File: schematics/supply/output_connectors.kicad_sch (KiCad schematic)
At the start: 16 parts, among them J16 banana jack + fuse 20A, J17 Conn_02x04_Odd_Even, J18 banana jack + fuse 15A, J19 jst xh angle, J20 jst xh angle, Q10 IRLML0030, Q10 IRLML5203

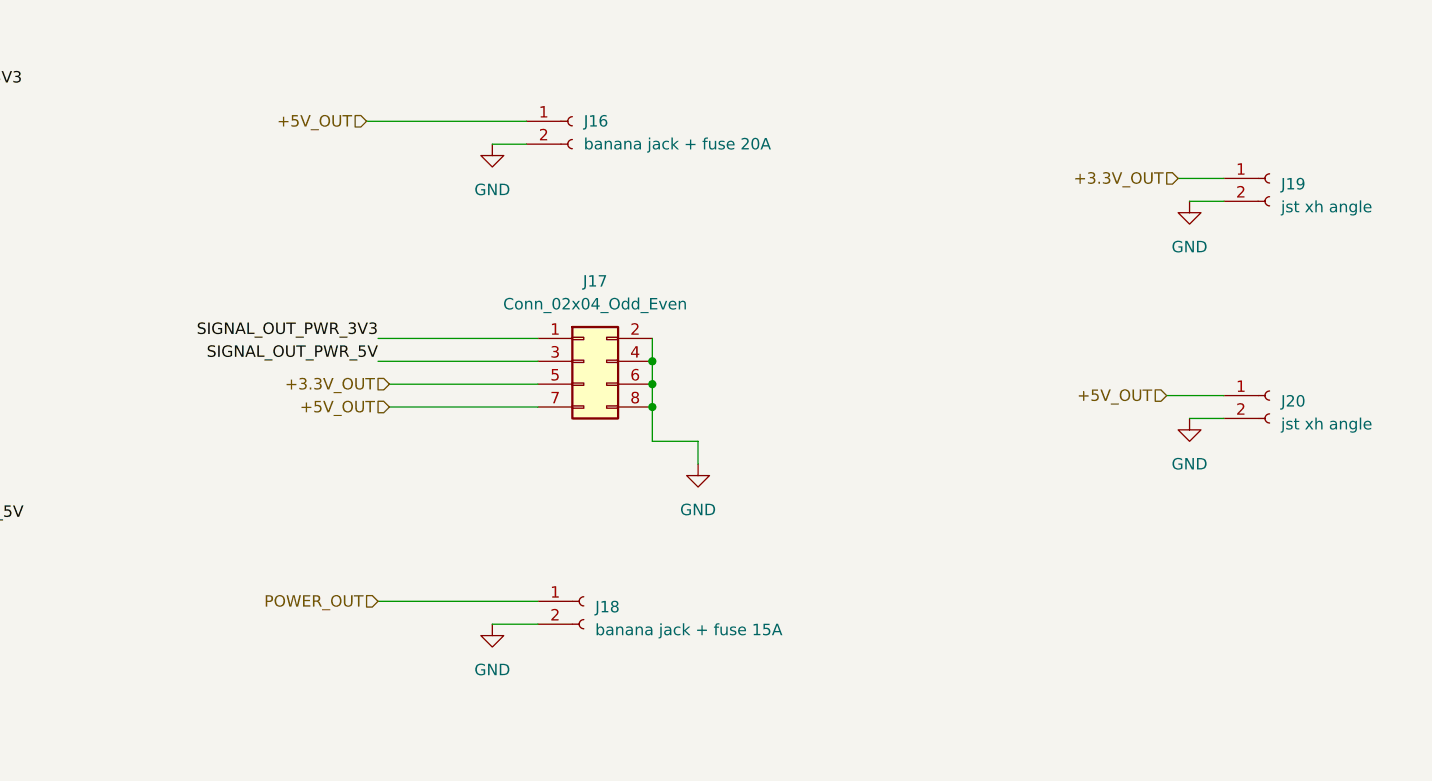
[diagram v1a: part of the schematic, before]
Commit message: Prepare to move USB ports to a few millimenters outside
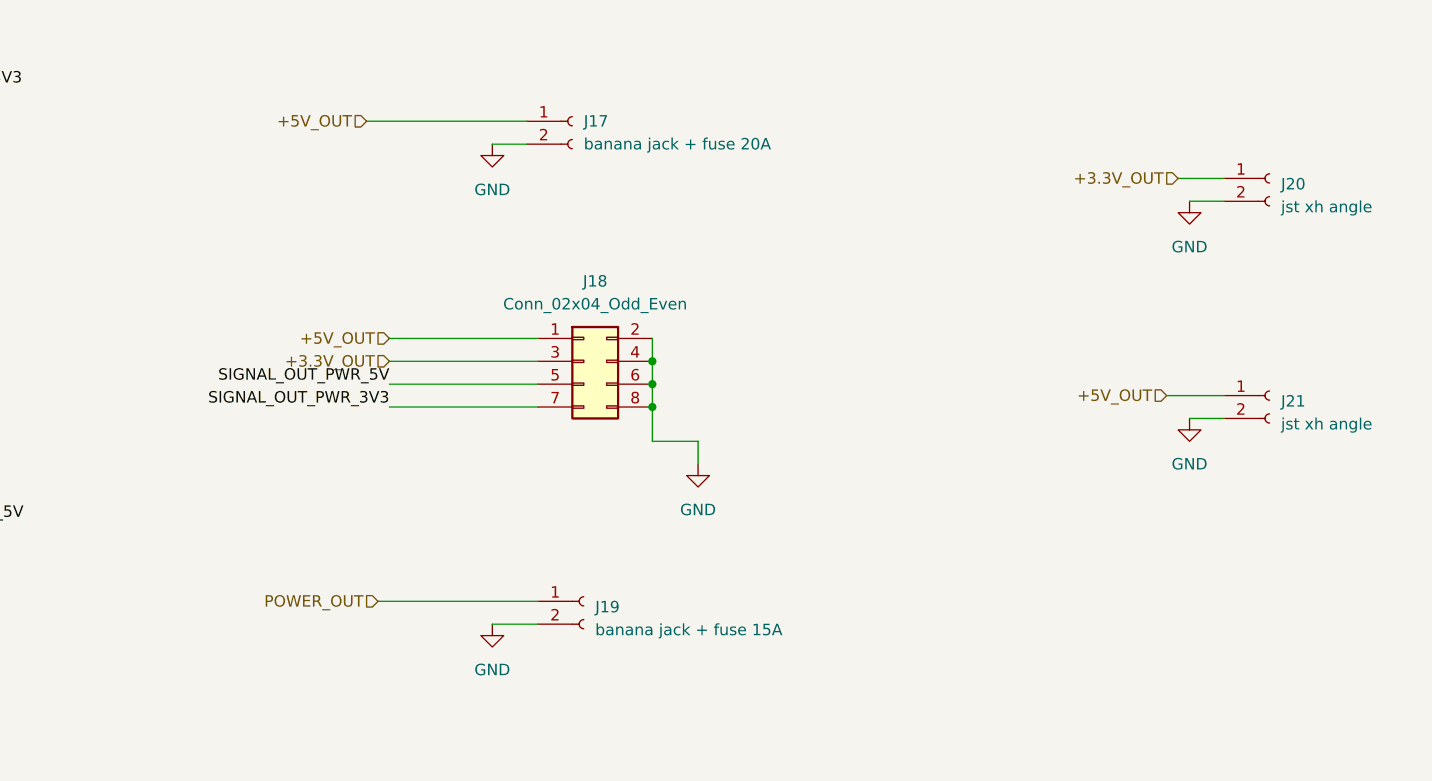
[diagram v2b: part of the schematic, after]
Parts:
- J18: renamed from J17; footprint Connector_PinHeader_2.54mm:PinHeader_2x04_P2.54mm_Vertical -> Connector_PinSocket_2.54mm:PinSocket_2x04_P2.54mm_Horizontal
- renumbered J16 to J17, J18 to J19, J19 to J20, J20 to J21
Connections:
- net +3.3V_OUT: now also J18.3 (Pin_3); no longer J18.5 (Pin_5)
- net +5V_OUT: now also J18.1 (Pin_1); no longer J18.7 (Pin_7)
- net SIGNAL_OUT_PWR_3V3: now also J18.7 (Pin_7); no longer J18.1 (Pin_1)
- net SIGNAL_OUT_PWR_5V: now also J18.5 (Pin_5); no longer J18.3 (Pin_3)

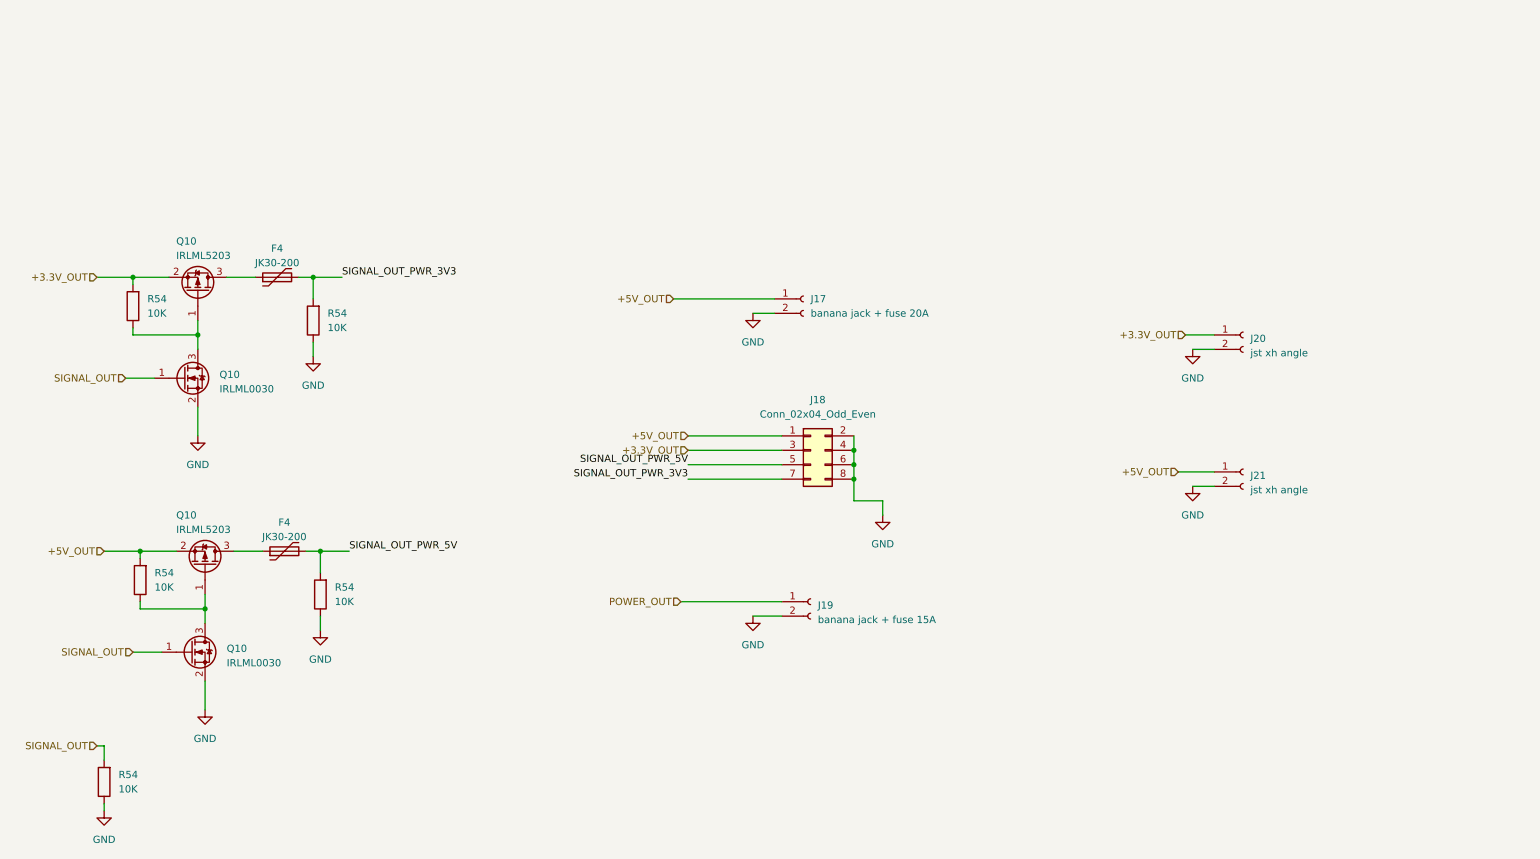
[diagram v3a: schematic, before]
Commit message: prepare to add current measurement for a middle-current 5V and 3.3V lines
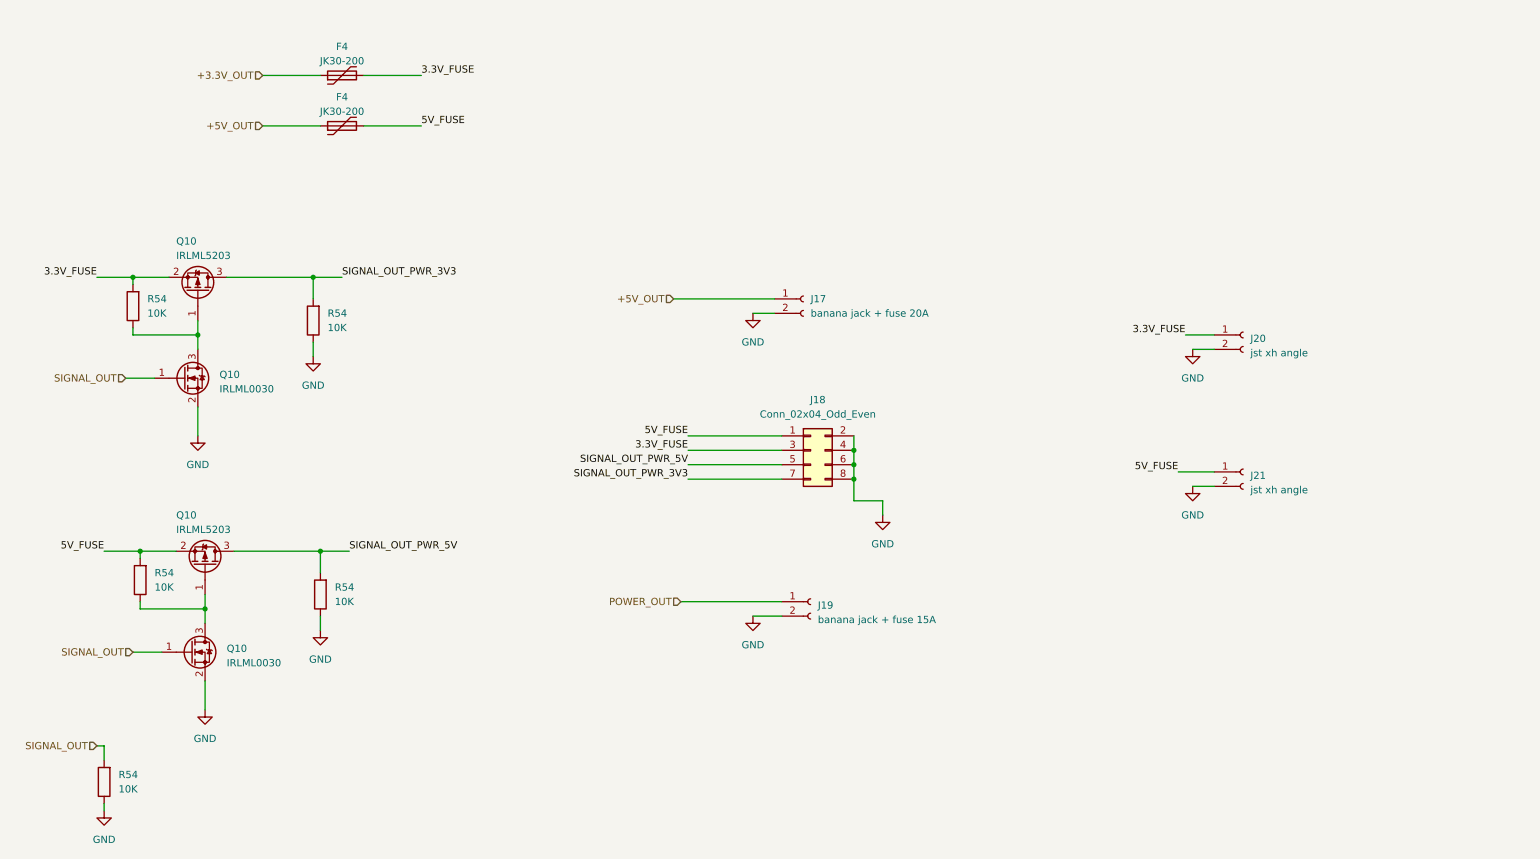
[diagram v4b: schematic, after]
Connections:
- net +3.3V_OUT: now also F4.1; no longer J18.3 (Pin_3), J20.1 (Pin_1), Q10.2 (S), R54.2
- net +5V_OUT: now also F4.1; no longer J18.1 (Pin_1), J21.1 (Pin_1), Q10.2 (S), R54.2
- net SIGNAL_OUT_PWR_3V3: now also Q10.3 (D); no longer F4.2
- net SIGNAL_OUT_PWR_5V: now also Q10.3 (D); no longer F4.2
- new net 3.3V_FUSE: F4.2, J18.3 (Pin_3), J20.1 (Pin_1), Q10.2 (S), R54.2
- new net 5V_FUSE: F4.2, J18.1 (Pin_1), J21.1 (Pin_1), Q10.2 (S), R54.2
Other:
- moved on the sheet: F4
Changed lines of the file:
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@@
   (junction (at 38.1 111.76) (diameter 0) (color 0 0 0 0)
   )
+  (junction (at 68.58 63.5) (diameter 0) (color 0 0 0 0)
+  )
   (junction (at 163.83 99.06) (diameter 0) (color 0 0 0 0)
   )
   (junction (at 163.83 96.52) (diameter 0) (color 0 0 0 0)
   )
-  (junction (at 68.58 63.5) (diameter 0) (color 0 0 0 0)
-  )
   (junction (at 49.53 121.92) (diameter 0) (color 0 0 0 0)
   )
@@
     (stroke (width 0) (type default))
   )
-  (wire (pts (xy 54.61 111.76) (xy 59.69 111.76))
+  (wire (pts (xy 59.69 36.83) (xy 69.85 36.83))
     (stroke (width 0) (type default))
   )
@@
     (stroke (width 0) (type default))
   )
+  (wire (pts (xy 54.61 111.76) (xy 69.85 111.76))
+    (stroke (width 0) (type default))
+  )
   (wire (pts (xy 134.62 91.44) (xy 151.13 91.44))
     (stroke (width 0) (type default))
@@
     (stroke (width 0) (type default))
   )
+  (wire (pts (xy 59.69 27.94) (xy 69.85 27.94))
+    (stroke (width 0) (type default))
+  )
   (wire (pts (xy 68.58 63.5) (xy 73.66 63.5))
     (stroke (width 0) (type default))
@@
     (stroke (width 0) (type default))
   )
+  (wire (pts (xy 77.47 27.94) (xy 87.63 27.94))
+    (stroke (width 0) (type default))
+  )
   (wire (pts (xy 223.52 100.33) (xy 227.33 100.33))
     (stroke (width 0) (type default))
@@
     (stroke (width 0) (type default))
   )
-  (wire (pts (xy 53.34 63.5) (xy 58.42 63.5))
-    (stroke (width 0) (type default))
-  )
   (wire (pts (xy 30.48 63.5) (xy 36.83 63.5))
     (stroke (width 0) (type default))
@@
     (stroke (width 0) (type default))
   )
+  (wire (pts (xy 53.34 63.5) (xy 68.58 63.5))
+    (stroke (width 0) (type default))
+  )
   (wire (pts (xy 48.26 86.36) (xy 48.26 91.44))
     (stroke (width 0) (type default))
   )
-  (wire (pts (xy 67.31 111.76) (xy 69.85 111.76))
+  (wire (pts (xy 69.85 111.76) (xy 74.93 111.76))
     (stroke (width 0) (type default))
   )
@@
     (stroke (width 0) (type default))
   )
-  (wire (pts (xy 69.85 111.76) (xy 74.93 111.76))
+  (wire (pts (xy 77.47 36.83) (xy 87.63 36.83))
     (stroke (width 0) (type default))
   )
@@
     (stroke (width 0) (type default))
   )
-  (wire (pts (xy 66.04 63.5) (xy 68.58 63.5))
-    (stroke (width 0) (type default))
-  )
   (wire (pts (xy 49.53 134.62) (xy 49.53 139.7))
     (stroke (width 0) (type default))
@@
   (wire (pts (xy 38.1 121.92) (xy 49.53 121.92))
     (stroke (width 0) (type default))
+  )
+  (label "5V_FUSE" (at 134.62 91.44 180) (fields_autoplaced)
+    (effects (font (size 1.27 1.27)) (justify right bottom))
   )
   (label "SIGNAL_OUT_PWR_5V" (at 134.62 96.52 180) (fields_autoplaced)
     (effects (font (size 1.27 1.27)) (justify right bottom))
   )
+  (label "5V_FUSE" (at 220.98 97.79 180) (fields_autoplaced)
+    (effects (font (size 1.27 1.27)) (justify right bottom))
+  )
+  (label "3.3V_FUSE" (at 30.48 63.5 180) (fields_autoplaced)
+    (effects (font (size 1.27 1.27)) (justify right bottom))
+  )
+  (label "3.3V_FUSE" (at 134.62 93.98 180) (fields_autoplaced)
+    (effects (font (size 1.27 1.27)) (justify right bottom))
+  )
   (label "SIGNAL_OUT_PWR_3V3" (at 73.66 63.5 0) (fields_autoplaced)
     (effects (font (size 1.27 1.27)) (justify left bottom))
   )
+  (label "5V_FUSE" (at 31.75 111.76 180) (fields_autoplaced)
+    (effects (font (size 1.27 1.27)) (justify right bottom))
+  )
+  (label "5V_FUSE" (at 87.63 36.83 0) (fields_autoplaced)
+    (effects (font (size 1.27 1.27)) (justify left bottom))
+  )
+  (label "3.3V_FUSE" (at 87.63 27.94 0) (fields_autoplaced)
+    (effects (font (size 1.27 1.27)) (justify left bottom))
+  )
   (label "SIGNAL_OUT_PWR_3V3" (at 134.62 99.06 180) (fields_autoplaced)
     (effects (font (size 1.27 1.27)) (justify right bottom))
@@
     (effects (font (size 1.27 1.27)) (justify left bottom))
   )
-  (hierarchical_label "+5V_OUT" (shape input) (at 220.98 97.79 180) (fields_autoplaced)
+  (label "3.3V_FUSE" (at 222.25 73.66 180) (fields_autoplaced)
+    (effects (font (size 1.27 1.27)) (justify right bottom))
+  )
+  (hierarchical_label "+5V_OUT" (shape input) (at 59.69 36.83 180) (fields_autoplaced)
     (effects (font (size 1.27 1.27)) (justify right))
   )
@@
     (effects (font (size 1.27 1.27)) (justify right))
   )
-  (hierarchical_label "+3.3V_OUT" (shape input) (at 30.48 63.5 180) (fields_autoplaced)
-    (effects (font (size 1.27 1.27)) (justify right))
-  )
   (hierarchical_label "SIGNAL_OUT" (shape input) (at 35.56 81.28 180) (fields_autoplaced)
     (effects (font (size 1.27 1.27)) (justify right))
   )
-  (hierarchical_label "+3.3V_OUT" (shape input) (at 134.62 93.98 180) (fields_autoplaced)
-    (effects (font (size 1.27 1.27)) (justify right))
-  )
   (hierarchical_label "SIGNAL_OUT" (shape input) (at 30.48 146.05 180) (fields_autoplaced)
     (effects (font (size 1.27 1.27)) (justify right))
   )
-  (hierarchical_label "+5V_OUT" (shape input) (at 31.75 111.76 180) (fields_autoplaced)
-    (effects (font (size 1.27 1.27)) (justify right))
-  )
   (hierarchical_label "SIGNAL_OUT" (shape input) (at 36.83 129.54 180) (fields_autoplaced)
     (effects (font (size 1.27 1.27)) (justify right))
   )
-  (hierarchical_label "+5V_OUT" (shape input) (at 134.62 91.44 180) (fields_autoplaced)
-    (effects (font (size 1.27 1.27)) (justify right))
-  )
-  (hierarchical_label "+3.3V_OUT" (shape input) (at 222.25 73.66 180) (fields_autoplaced)
+  (hierarchical_label "+3.3V_OUT" (shape input) (at 59.69 27.94 180) (fields_autoplaced)
     (effects (font (size 1.27 1.27)) (justify right))
   )
@@
     )
   )
-  (symbol (lib_id "Device:Polyfuse") (at 62.23 63.5 90) (unit 1)
-    (in_bom yes) (on_board yes) (dnp no) (fields_autoplaced)
-    (property "Reference" "F4" (at 62.23 58.42 90)
-      (effects (font (size 1.27 1.27)))
-    )
-    (property "Value" "JK30-200" (at 62.23 60.96 90)
-      (effects (font (size 1.27 1.27)))
-    )
-    (property "Footprint" "Capacitor_THT:C_Disc_D11.0mm_W5.0mm_P5.00mm" (at 67.31 62.23 0)
+  (symbol (lib_id "Device:Polyfuse") (at 73.66 27.94 90) (unit 1)
+    (in_bom yes) (on_board yes) (dnp no) (fields_autoplaced)
+    (property "Reference" "F4" (at 73.66 22.86 90)
+      (effects (font (size 1.27 1.27)))
+    )
+    (property "Value" "JK30-200" (at 73.66 25.4 90)
+      (effects (font (size 1.27 1.27)))
+    )
+    (property "Footprint" "Capacitor_THT:C_Disc_D11.0mm_W5.0mm_P5.00mm" (at 78.74 26.67 0)
       (effects (font (size 1.27 1.27)) (justify left) hide)
     )
-    (property "Datasheet" "~" (at 62.23 63.5 0)
+    (property "Datasheet" "~" (at 73.66 27.94 0)
       (effects (font (size 1.27 1.27)) hide)
     )
@@
     )
   )
-  (symbol (lib_id "Device:Polyfuse") (at 63.5 111.76 90) (unit 1)
-    (in_bom yes) (on_board yes) (dnp no) (fields_autoplaced)
-    (property "Reference" "F4" (at 63.5 106.68 90)
-      (effects (font (size 1.27 1.27)))
-    )
-    (property "Value" "JK30-200" (at 63.5 109.22 90)
-      (effects (font (size 1.27 1.27)))
-    )
-    (property "Footprint" "Capacitor_THT:C_Disc_D11.0mm_W5.0mm_P5.00mm" (at 68.58 110.49 0)
+  (symbol (lib_id "Device:Polyfuse") (at 73.66 36.83 90) (unit 1)
+    (in_bom yes) (on_board yes) (dnp no) (fields_autoplaced)
+    (property "Reference" "F4" (at 73.66 31.75 90)
+      (effects (font (size 1.27 1.27)))
+    )
+    (property "Value" "JK30-200" (at 73.66 34.29 90)
+      (effects (font (size 1.27 1.27)))
+    )
+    (property "Footprint" "Capacitor_THT:C_Disc_D11.0mm_W5.0mm_P5.00mm" (at 78.74 35.56 0)
       (effects (font (size 1.27 1.27)) (justify left) hide)
     )
-    (property "Datasheet" "~" (at 63.5 111.76 0)
-      (effects (font (size 1.27 1.27)) hide)
-    )
+    (property "Datasheet" "~" (at 73.66 36.83 0)
+      (effects (font (size 1.27 1.27)) hide)
+    )

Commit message: prepare to replace inductor on 5V power line
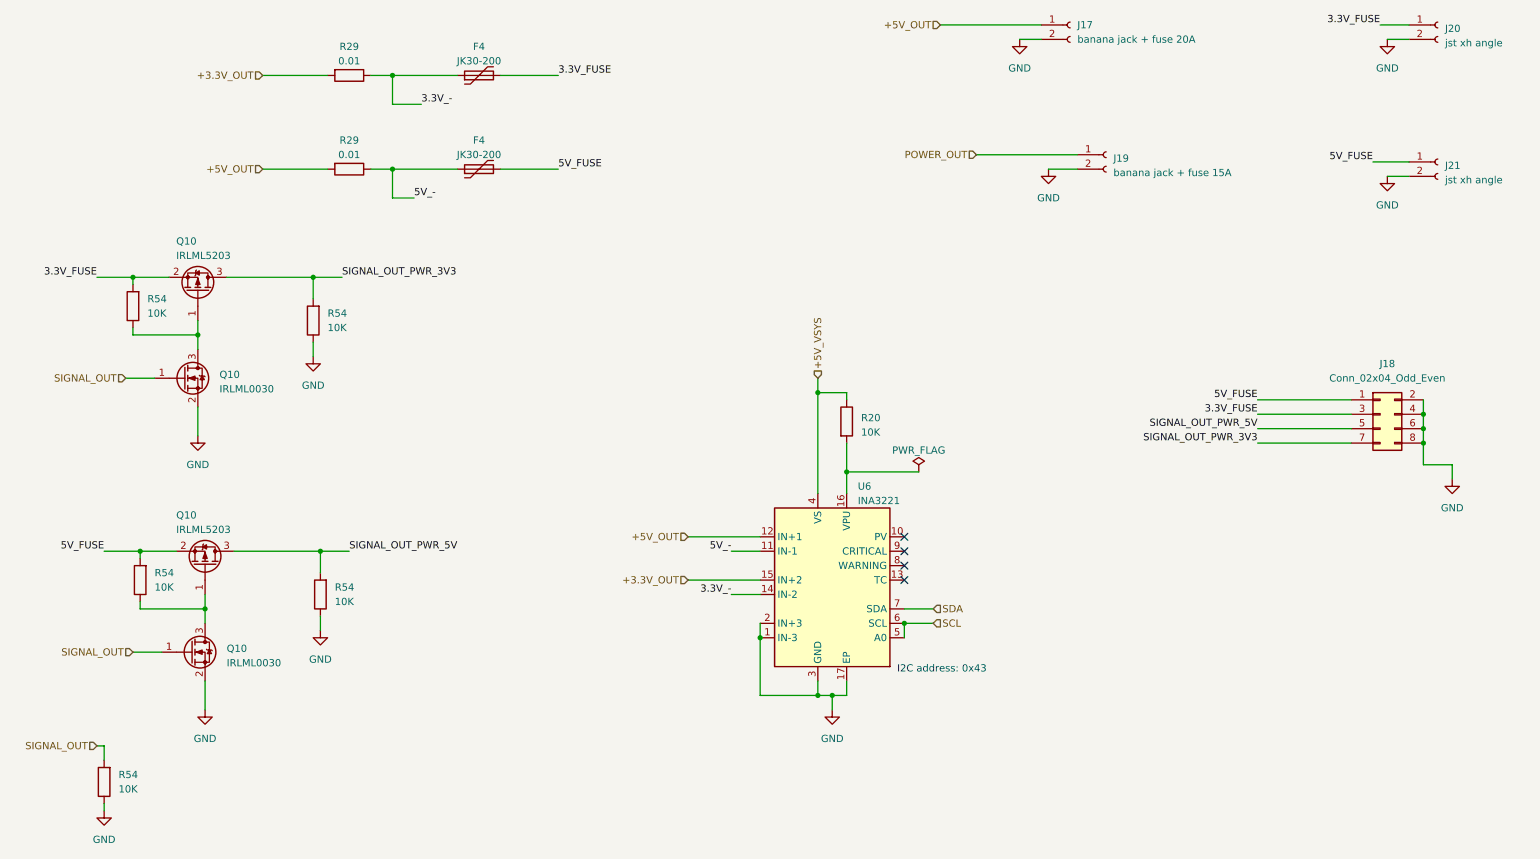
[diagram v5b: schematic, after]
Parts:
- added R20: 10K, Resistor_SMD:R_0805_2012Metric, symbol Device:R
- added R29 (x2): 0.01, Resistor_SMD:R_1206_3216Metric, symbol Device:R
- added U6: INA3221, Package_DFN_QFN:Texas_RGV_S-PVQFN-N16_EP2.1x2.1mm, symbol Power_Management:INA3221
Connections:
- net +3.3V_OUT: now also R29.2, U6.15 (IN+2); no longer F4.1
- net +5V_OUT: now also R29.2, U6.12 (IN+1); no longer F4.1
- net GND: now also U6.1 (IN-3), U6.17 (EP), U6.2 (IN+3), U6.3 (GND)
- new net: R20.2, U6.16 (VPU)
- new net +5V_VSYS: R20.1, U6.4 (VS)
- new net 3.3V_-: F4.1, R29.1, U6.14 (IN-2)
- new net 5V_-: F4.1, R29.1, U6.11 (IN-1)
- new net SCL: U6.5 (A0), U6.6 (SCL)
- new net SDA: U6.7 (SDA)
- no-connect marks 0 -> 4
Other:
- note added: "I2C address: 0x43"
- moved on the sheet: F4, J17, J18, J19, J20, J21
